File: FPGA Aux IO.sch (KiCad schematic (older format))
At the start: 3 parts

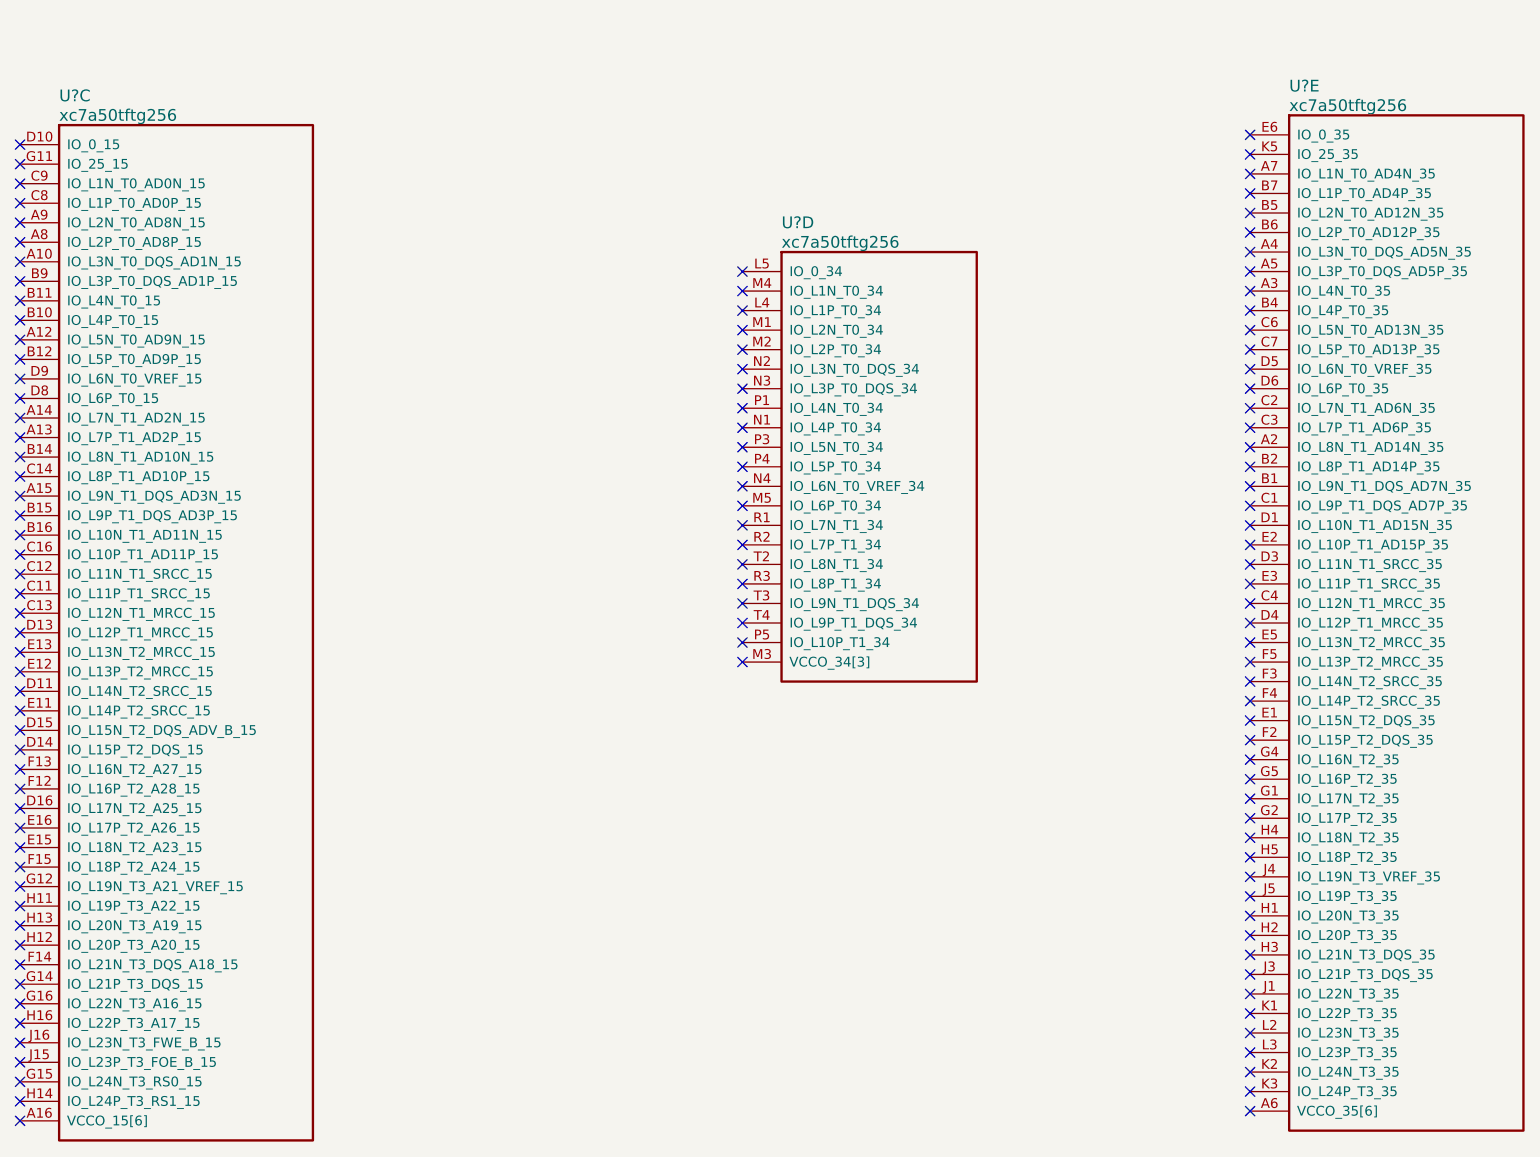
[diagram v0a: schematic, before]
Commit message: added HDMI, moved rotary encoders to USBSPI gpio
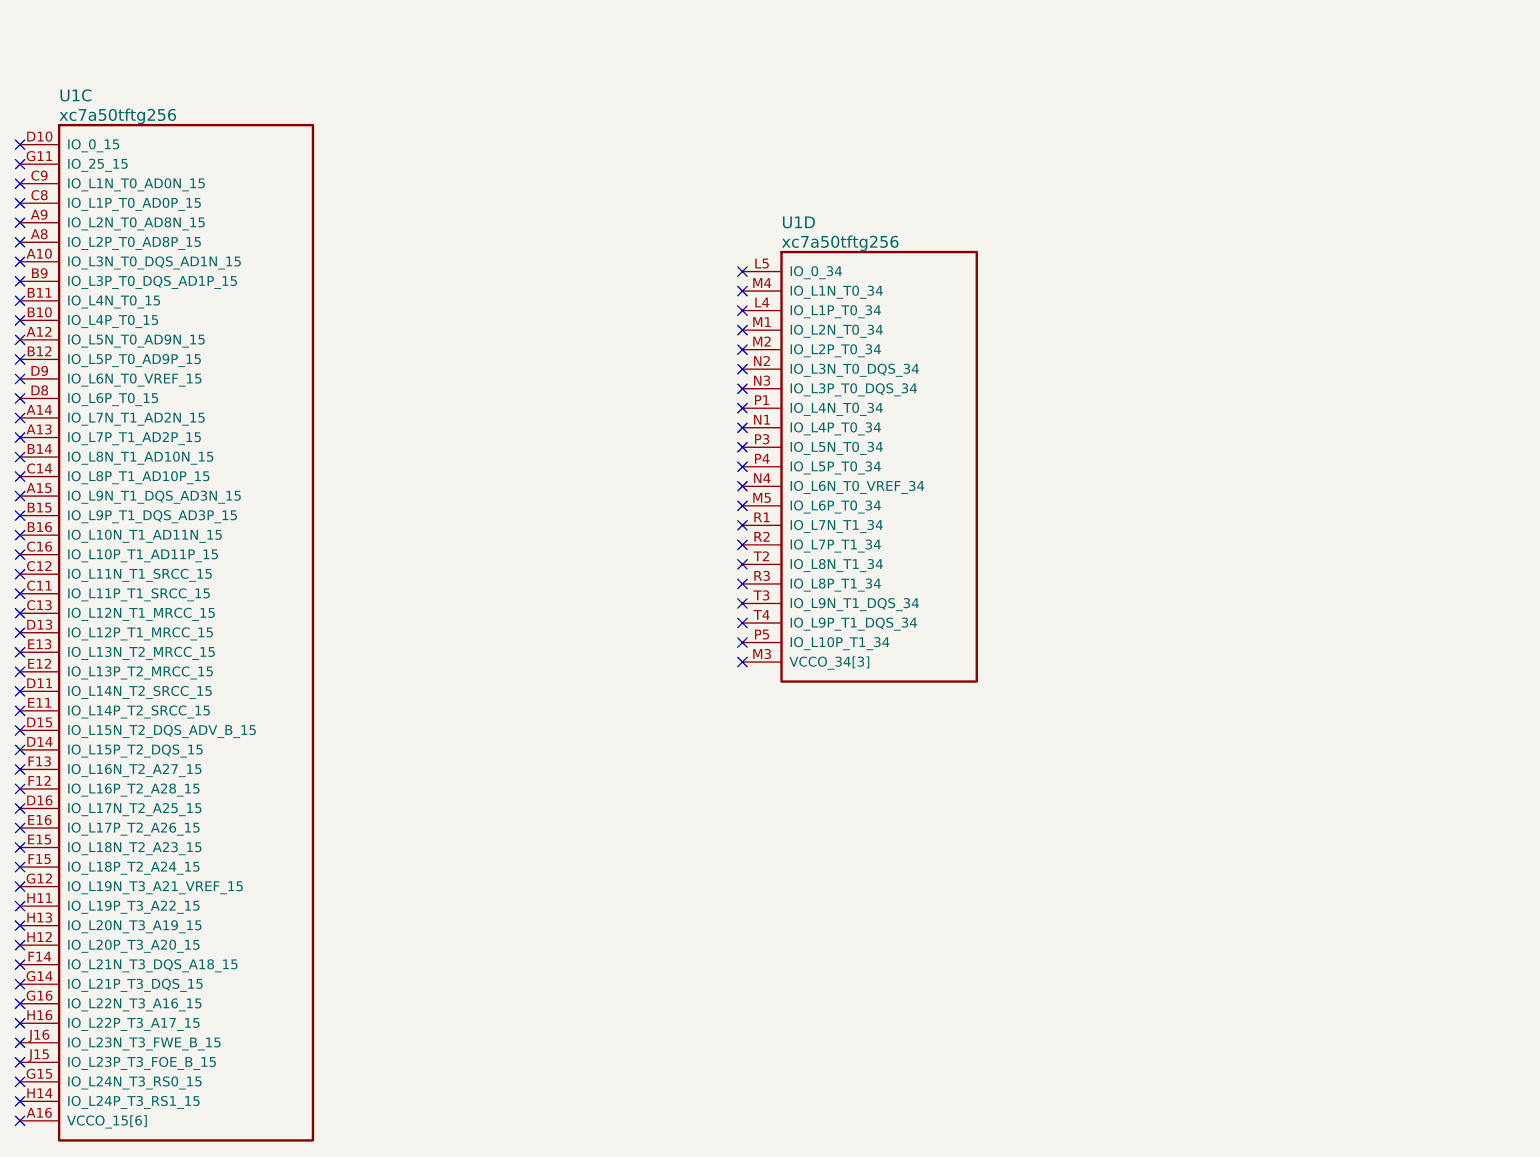
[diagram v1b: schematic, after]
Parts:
- removed U?: xc7a50tftg256, symbol xc7a50tftg256
- gave numbers to parts that had none: 1
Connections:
- no-connect marks 123 -> 72
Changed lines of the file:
@@
 LIBS:usb_condom_extended_v1-cache
 LIBS:tinkerforge
+LIBS:si570
+LIBS:hdmi_BiDir_n
 EELAYER 25 0
 EELAYER END
 $Descr A4 11693 8268
 encoding utf-8
-Sheet 6 13
+Sheet 6 14
 Title ""
 Date ""
@@
 $EndDescr
 $Comp
-L xc7a50tftg256 U?
+L xc7a50tftg256 U1
 U 3 1 585C5883
 P 1850 1450
-F 0 "U?" H 2050 1700 60  0000 L CNN
+F 0 "U1" H 2050 1700 60  0000 L CNN
 F 1 "xc7a50tftg256" H 2050 1600 60  0000 L CNN
 F 2 "" H 1850 1450 60  0001 C CNN
@@
 	1    0    0    -1
 $EndComp
-$Comp
-L xc7a50tftg256 U?
-U 5 1 585C595B
-P 8150 1400
-F 0 "U?" H 8350 1650 60  0000 L CNN
-F 1 "xc7a50tftg256" H 8350 1550 60  0000 L CNN
-F 2 "" H 8150 1400 60  0001 C CNN
-F 3 "" H 8150 1400 60  0001 C CNN
-	5    8150 1400
-	1    0    0    -1
-$EndComp
-NoConn ~ 8150 1400
-NoConn ~ 8150 1500
-NoConn ~ 8150 1600
-NoConn ~ 8150 1700
-NoConn ~ 8150 1800
-NoConn ~ 8150 3100
-NoConn ~ 8150 3200
-NoConn ~ 8150 3300
-NoConn ~ 8150 3400
-NoConn ~ 8150 3500
-NoConn ~ 8150 3600
-NoConn ~ 8150 1900
-NoConn ~ 8150 2000
-NoConn ~ 8150 2100
-NoConn ~ 8150 2200
-NoConn ~ 8150 2300
-NoConn ~ 8150 2400
-NoConn ~ 8150 3700
-NoConn ~ 8150 3800
-NoConn ~ 8150 3900
-NoConn ~ 8150 4000
-NoConn ~ 8150 4100
-NoConn ~ 8150 4200
-NoConn ~ 8150 4300
-NoConn ~ 8150 4400
-NoConn ~ 8150 4500
-NoConn ~ 8150 4600
-NoConn ~ 8150 4700
-NoConn ~ 8150 4800
-NoConn ~ 8150 4900
-NoConn ~ 8150 5000
-NoConn ~ 8150 5100
-NoConn ~ 8150 5200
-NoConn ~ 8150 5300
-NoConn ~ 8150 5400
-NoConn ~ 8150 2500
-NoConn ~ 8150 2600
-NoConn ~ 8150 2700
-NoConn ~ 8150 2800
-NoConn ~ 8150 2900
-NoConn ~ 8150 3000
-NoConn ~ 8150 5500
-NoConn ~ 8150 5600
-NoConn ~ 8150 5700
-NoConn ~ 8150 5800
-NoConn ~ 8150 5900
-NoConn ~ 8150 6000
-NoConn ~ 8150 6100
-NoConn ~ 8150 6200
-NoConn ~ 8150 6300
-NoConn ~ 8150 6400
 NoConn ~ 5550 2100
 NoConn ~ 5550 2200
@@
 NoConn ~ 1850 6450
 $Comp
-L xc7a50tftg256 U?
+L xc7a50tftg256 U1
 U 4 1 585C58DC
 P 5550 2100
-F 0 "U?" H 5750 2350 60  0000 L CNN
+F 0 "U1" H 5750 2350 60  0000 L CNN
 F 1 "xc7a50tftg256" H 5750 2250 60  0000 L CNN
 F 2 "" H 5550 2100 60  0001 C CNN

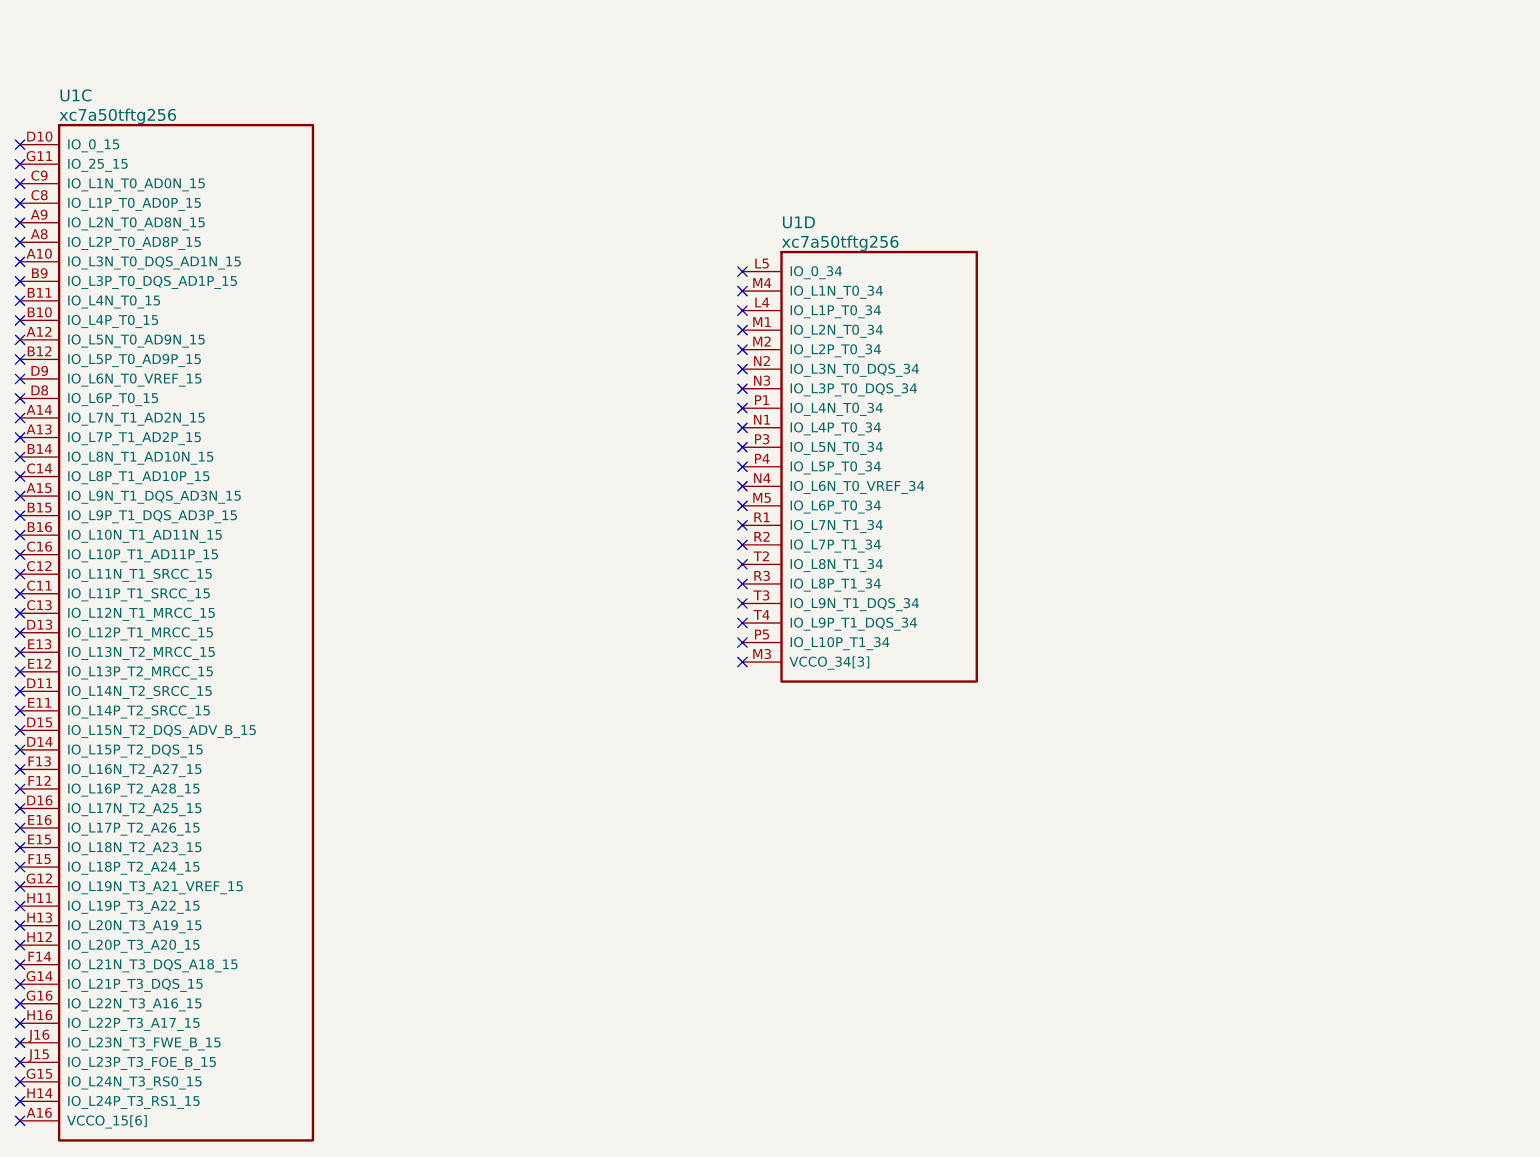
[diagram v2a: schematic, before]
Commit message: a few changes persuant to FX3 PCB design recommendations
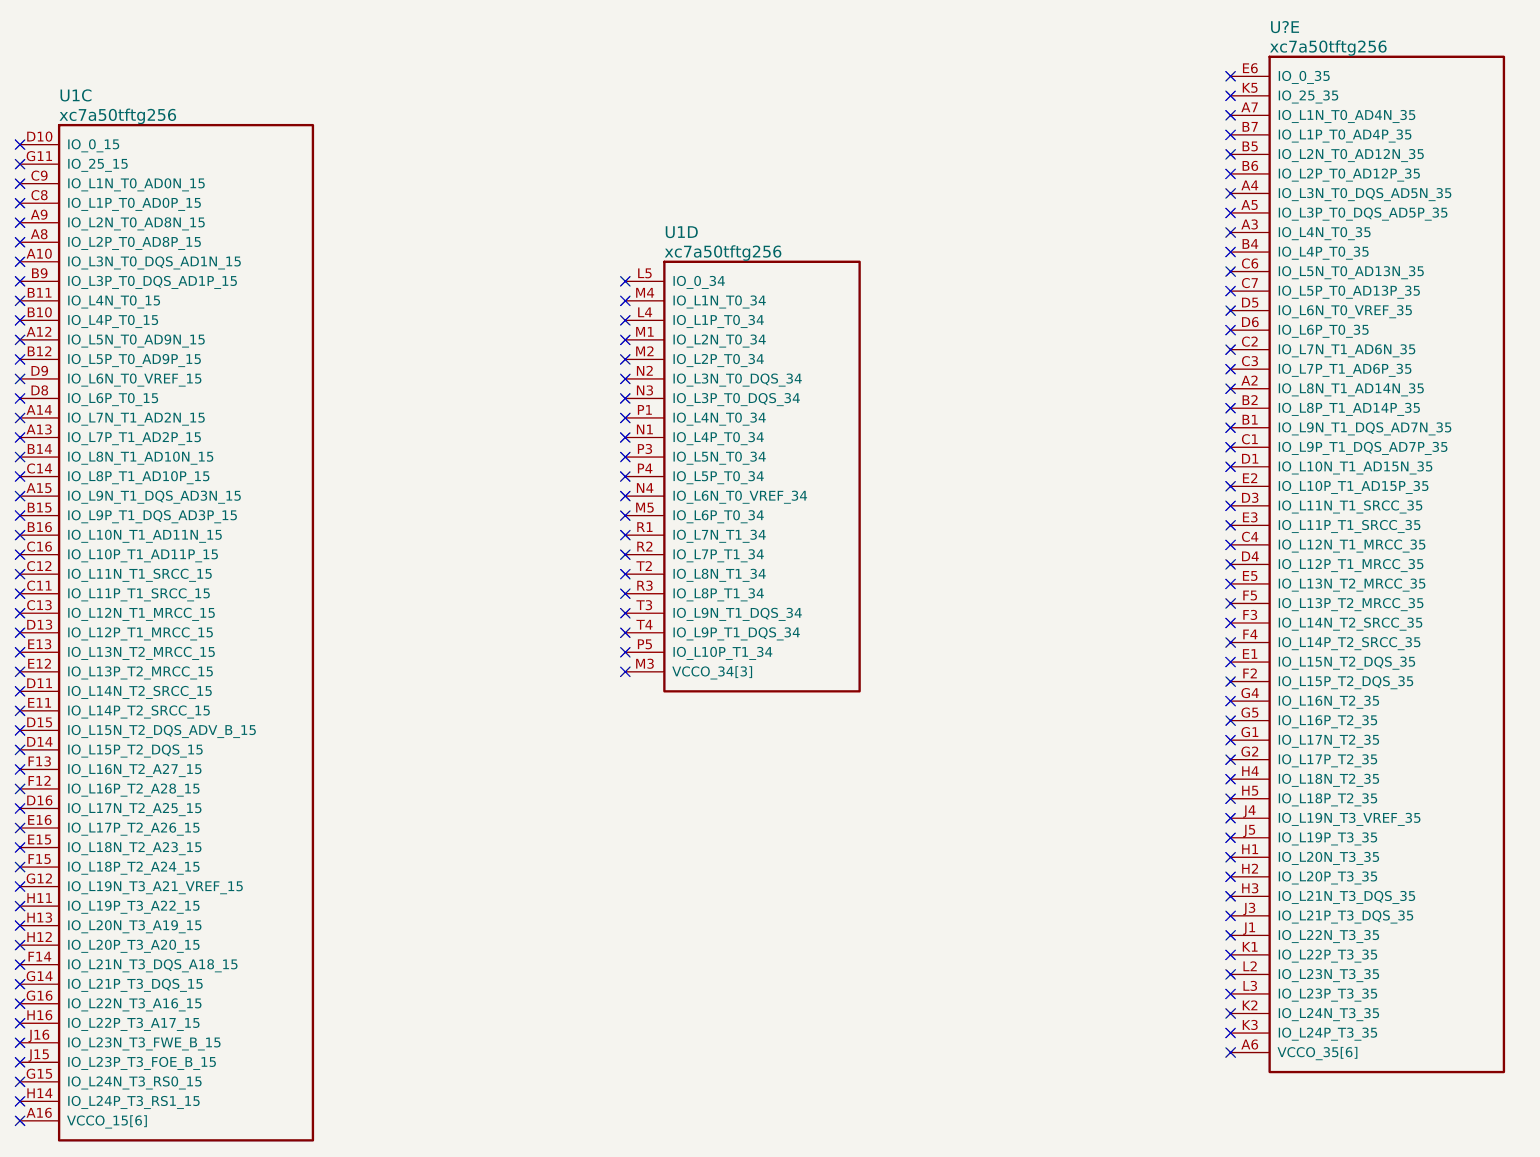
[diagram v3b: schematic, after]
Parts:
- added U?: xc7a50tftg256, symbol xc7a50tftg256
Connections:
- new net: U?.A6 (VCCO_35[6]), U?.B3 (VCCO_35[6]), U?.D7 (VCCO_35[6]), U?.E4 (VCCO_35[6]), U?.F1 (VCCO_35[6]), U?.J2 (VCCO_35[6])
- no-connect marks 72 -> 123
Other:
- moved on the sheet: U1D
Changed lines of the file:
@@
 $Descr A4 11693 8268
 encoding utf-8
-Sheet 6 14
+Sheet 6 13
 Title ""
 Date ""
@@
 	1    0    0    -1
 $EndComp
-NoConn ~ 5550 2100
-NoConn ~ 5550 2200
-NoConn ~ 5550 2300
-NoConn ~ 5550 2400
-NoConn ~ 5550 2500
-NoConn ~ 5550 2600
-NoConn ~ 5550 2700
-NoConn ~ 5550 2800
-NoConn ~ 5550 3900
-NoConn ~ 5550 4000
-NoConn ~ 5550 4100
-NoConn ~ 5550 2900
-NoConn ~ 5550 3000
-NoConn ~ 5550 3100
-NoConn ~ 5550 3200
-NoConn ~ 5550 3300
-NoConn ~ 5550 3400
-NoConn ~ 5550 3500
-NoConn ~ 5550 3600
-NoConn ~ 5550 3700
-NoConn ~ 5550 3800
+NoConn ~ 4950 2150
+NoConn ~ 4950 2250
+NoConn ~ 4950 2350
+NoConn ~ 4950 2450
+NoConn ~ 4950 2550
+NoConn ~ 4950 2650
+NoConn ~ 4950 2750
+NoConn ~ 4950 2850
+NoConn ~ 4950 3950
+NoConn ~ 4950 4050
+NoConn ~ 4950 4150
+NoConn ~ 4950 2950
+NoConn ~ 4950 3050
+NoConn ~ 4950 3150
+NoConn ~ 4950 3250
+NoConn ~ 4950 3350
+NoConn ~ 4950 3450
+NoConn ~ 4950 3550
+NoConn ~ 4950 3650
+NoConn ~ 4950 3750
+NoConn ~ 4950 3850
 NoConn ~ 1850 2450
 NoConn ~ 1850 2550
@@
 L xc7a50tftg256 U1
 U 4 1 585C58DC
-P 5550 2100
-F 0 "U1" H 5750 2350 60  0000 L CNN
-F 1 "xc7a50tftg256" H 5750 2250 60  0000 L CNN
-F 2 "" H 5550 2100 60  0001 C CNN
-F 3 "" H 5550 2100 60  0001 C CNN
-	4    5550 2100
+P 4950 2150
+F 0 "U1" H 5150 2400 60  0000 L CNN
+F 1 "xc7a50tftg256" H 5150 2300 60  0000 L CNN
+F 2 "" H 4950 2150 60  0001 C CNN
+F 3 "" H 4950 2150 60  0001 C CNN
+	4    4950 2150
 	1    0    0    -1
 $EndComp
+$Comp
+L xc7a50tftg256 U?
+U 5 1 5868B904
+P 8050 1100
+F 0 "U?" H 8250 1350 60  0000 L CNN
+F 1 "xc7a50tftg256" H 8250 1250 60  0000 L CNN
+F 2 "" H 8050 1100 60  0001 C CNN
+F 3 "" H 8050 1100 60  0001 C CNN
+	5    8050 1100
+	1    0    0    -1
+$EndComp
+NoConn ~ 8050 2100
+NoConn ~ 8050 2200
+NoConn ~ 8050 2300
+NoConn ~ 8050 2400
+NoConn ~ 8050 2500
+NoConn ~ 8050 2600
+NoConn ~ 8050 2700
+NoConn ~ 8050 2800
+NoConn ~ 8050 2900
+NoConn ~ 8050 3000
+NoConn ~ 8050 1100
+NoConn ~ 8050 1200
+NoConn ~ 8050 1300
+NoConn ~ 8050 1400
+NoConn ~ 8050 1500
+NoConn ~ 8050 1600
+NoConn ~ 8050 1700
+NoConn ~ 8050 1800
+NoConn ~ 8050 1900
+NoConn ~ 8050 2000
+NoConn ~ 8050 4100
+NoConn ~ 8050 4200
+NoConn ~ 8050 4300
+NoConn ~ 8050 4400
+NoConn ~ 8050 4500
+NoConn ~ 8050 4600
+NoConn ~ 8050 4700
+NoConn ~ 8050 4800
+NoConn ~ 8050 4900
+NoConn ~ 8050 5000
+NoConn ~ 8050 3100
+NoConn ~ 8050 3200
+NoConn ~ 8050 3300
+NoConn ~ 8050 3400
+NoConn ~ 8050 3500
+NoConn ~ 8050 3600
+NoConn ~ 8050 3700
+NoConn ~ 8050 3800
+NoConn ~ 8050 3900
+NoConn ~ 8050 4000
+NoConn ~ 8050 5100
+NoConn ~ 8050 5200
+NoConn ~ 8050 5300
+NoConn ~ 8050 5400
+NoConn ~ 8050 5500
+NoConn ~ 8050 5600
+NoConn ~ 8050 5700
+NoConn ~ 8050 5800
+NoConn ~ 8050 5900
+NoConn ~ 8050 6000
+NoConn ~ 8050 6100
 $EndSCHEMATC
